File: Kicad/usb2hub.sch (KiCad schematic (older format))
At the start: 2 parts

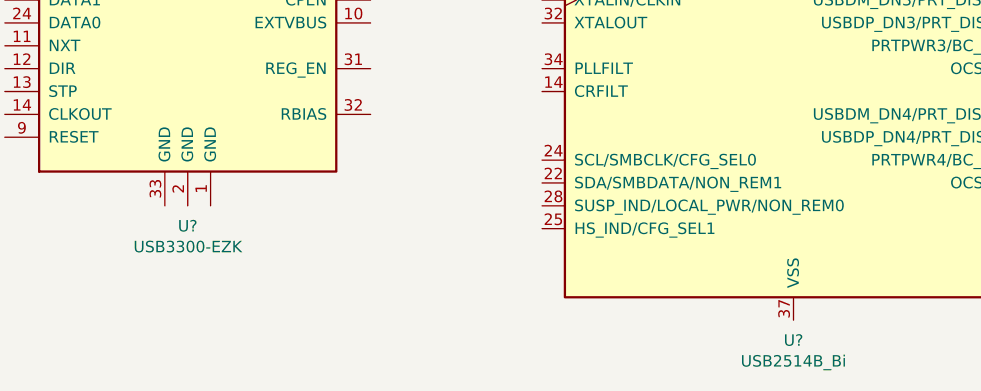
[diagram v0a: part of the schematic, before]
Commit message: Adding VGA output buffer/filter.
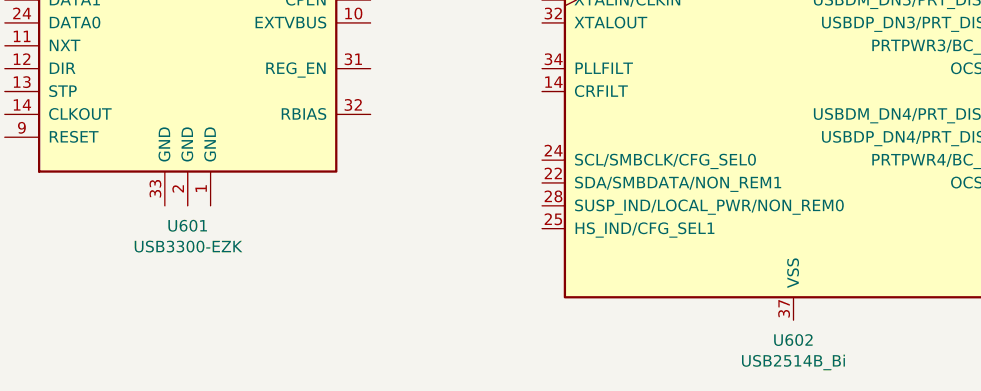
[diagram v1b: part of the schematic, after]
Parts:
- gave numbers to parts that had none: 2
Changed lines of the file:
@@
 P 5425 3575
 AR Path="/643FE60E" Ref="U?"  Part="1"
-AR Path="/64388AFF/643FE60E" Ref="U?"  Part="1"
-F 0 "U?" H 5425 2386 50  0000 C CNN
+AR Path="/64388AFF/643FE60E" Ref="U601"  Part="1"
+F 0 "U601" H 5425 2386 50  0000 C CNN
 F 1 "USB3300-EZK" H 5425 2295 50  0000 C CNN
 F 2 "Package_DFN_QFN:QFN-32-1EP_5x5mm_P0.5mm_EP3.45x3.45mm" H 6725 2325 50  0001 C CNN
@@
 $EndComp
 $Comp
-L Interface_USB:USB2514B_Bi U?
+L Interface_USB:USB2514B_Bi U602
 U 1 1 644028E0
 P 8075 3675
-F 0 "U?" H 8075 2086 50  0000 C CNN
+F 0 "U602" H 8075 2086 50  0000 C CNN
 F 1 "USB2514B_Bi" H 8075 1995 50  0000 C CNN
 F 2 "Package_DFN_QFN:QFN-36-1EP_6x6mm_P0.5mm_EP3.7x3.7mm" H 9375 2175 50  0001 C CNN

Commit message: Removed USB FS hub. Added stacked USB A connector.
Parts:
- added C? (x4): 100u, Capacitor_Tantalum_SMD:CP_EIA-3528-21_Kemet-B, symbol Device:CP
- added J?: USB_A_x2, symbol Neotron-528ST:USB_A_x2
- added J?: Conn_02x05_Top_Bottom, symbol Connector_Generic:Conn_02x05_Top_Bottom
- added U? (x4): AAT4610BIGV-1-T1, Package_TO_SOT_SMD:SOT-23-8, symbol Power_Management:AAT4610BIGV-1-T1
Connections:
- net labels added: +3.3V, +5V, DATA0, DATA1, DATA2, DATA3, DATA4, DATA5, DATA6, DATA7, DATA[7..0], GND, VBUS1, VBUS2, VBUS3, VBUS4, ~PORT1_EN, ~PORT1_OC, ~PORT2_EN, ~PORT2_OC, ~PORT3_EN, ~PORT3_OC, ~PORT4_EN, ~PORT4_OC
- wire segments 2 -> 123
- no-connect marks 0 -> 1
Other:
- note added: "USB 2.0 is 50 ohm\ndifferential pairs"
- note added: "Use PC-style internal USB2.0 10 pin socket to 2x USB A cable.\nPin 5 on this header is missing, to act as a key."
- moved on the sheet: U601, U602

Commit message: Swap to H7 in the Schematic
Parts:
- J?: symbol Neotron-528ST:USB_A_x2 -> Neotron-500:USB_A_x2
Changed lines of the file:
@@
 	2450 1975 2900 1975
 $Comp
-L Neotron-528ST:USB_A_x2 J?
+L Neotron-500:USB_A_x2 J?
 U 1 1 626FA669
 P 9100 2325

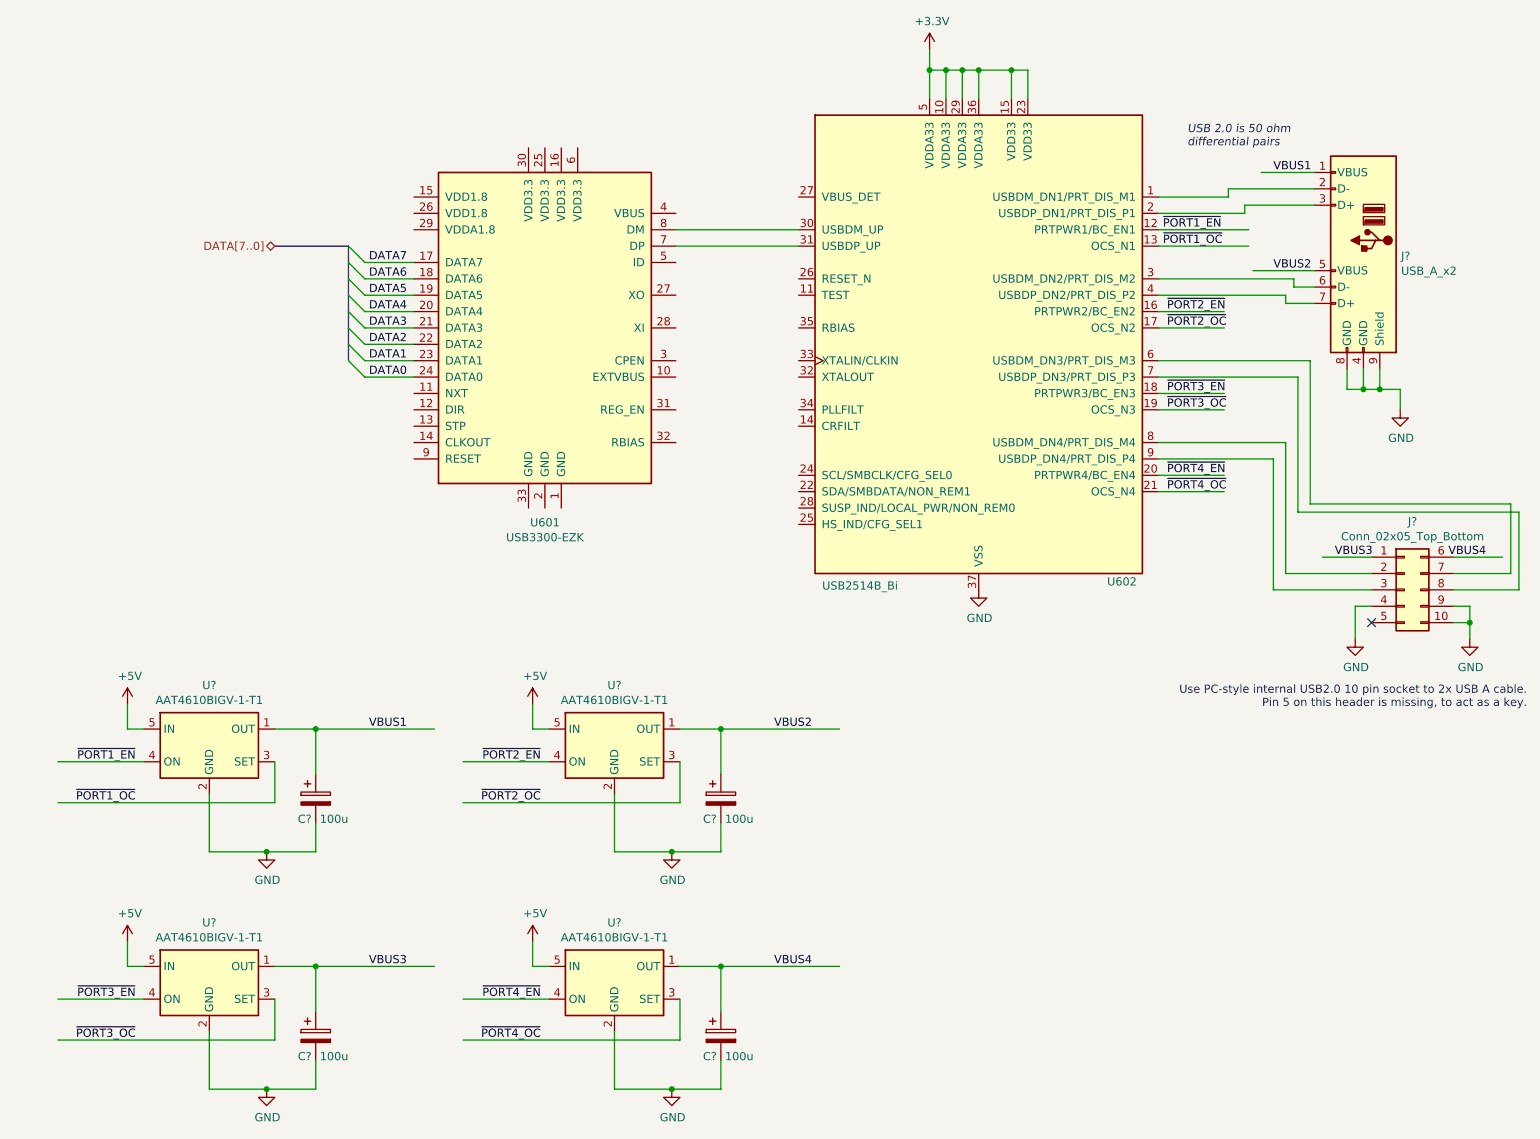
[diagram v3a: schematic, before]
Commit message: Schematic updates
Worked on USB Hub
Deleted QSPI SRAM
Added TSSOP-54 SDRAM (not wired up)
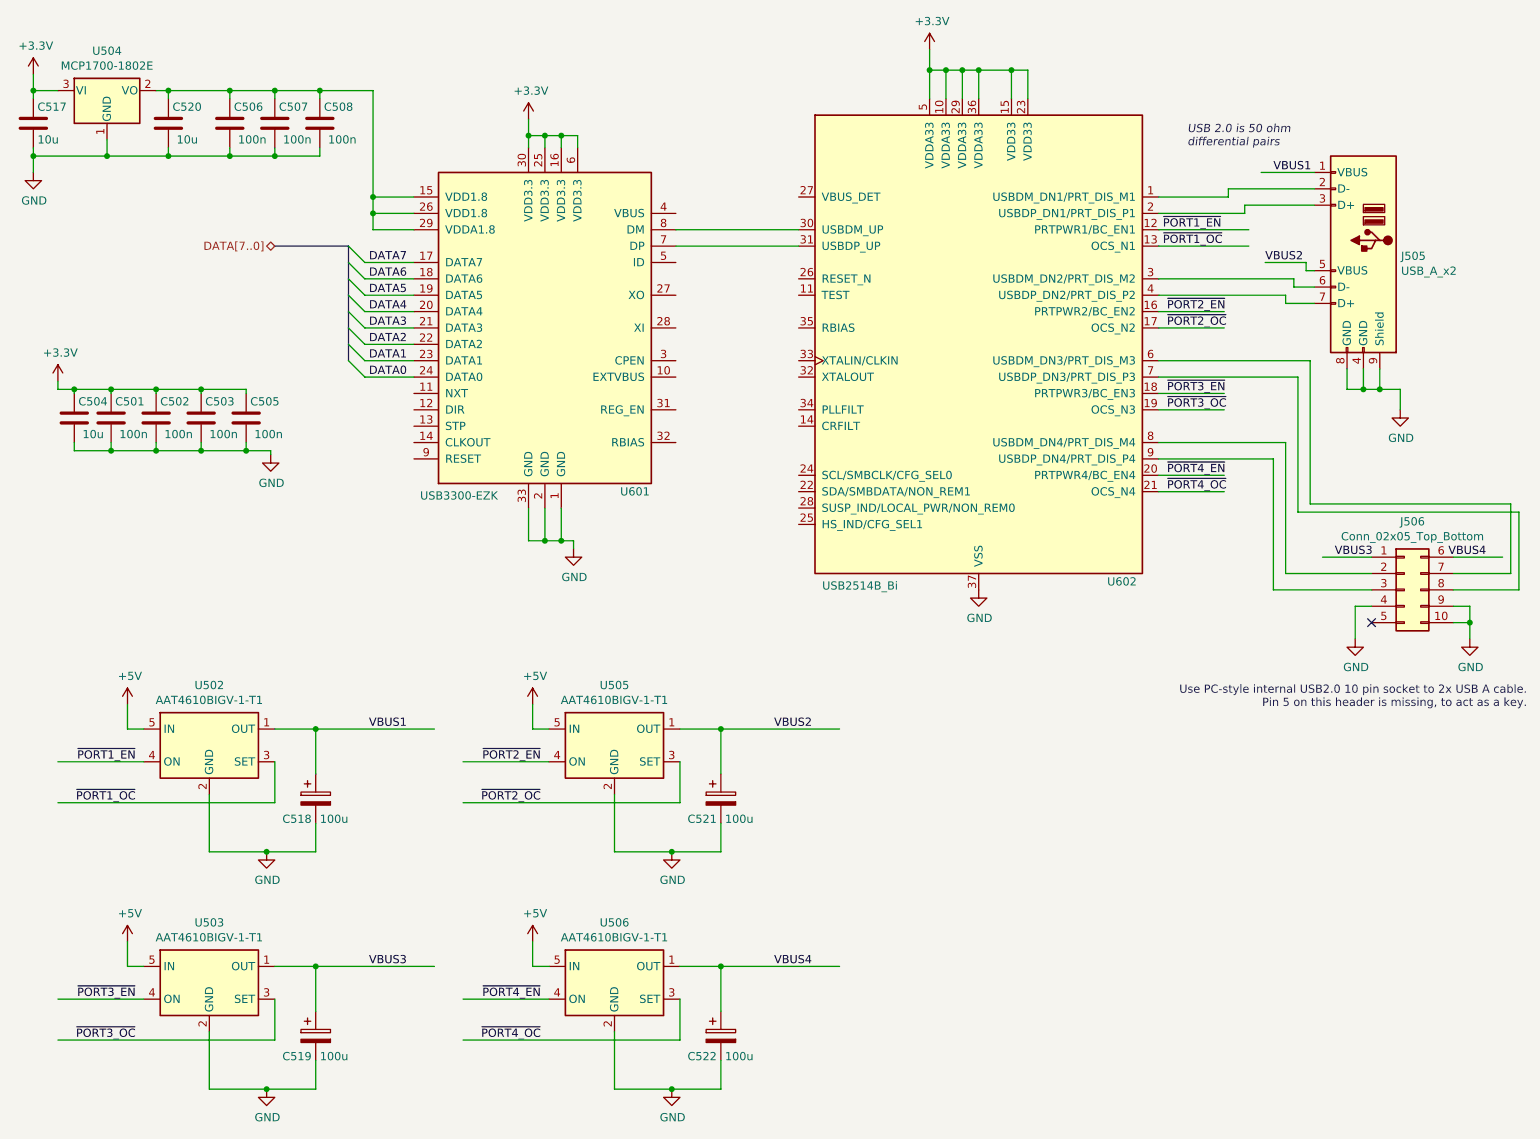
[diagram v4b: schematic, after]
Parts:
- added C501, C502, C503, C505, C506, C507, C508: 100n, symbol Device:C
- added C504, C517, C520: 10u, symbol Device:C
- added U504: MCP1700-1802E, Package_TO_SOT_SMD:SOT-23, symbol Regulator_Linear:MCP1700-1802E_SOT23
- gave numbers to parts that had none: 10
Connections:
- wire segments 123 -> 192
